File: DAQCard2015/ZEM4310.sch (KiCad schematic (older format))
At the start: 2 parts, among them P1 QTH-090-01-F-D-A, P2 QTH-090-01-F-D-A

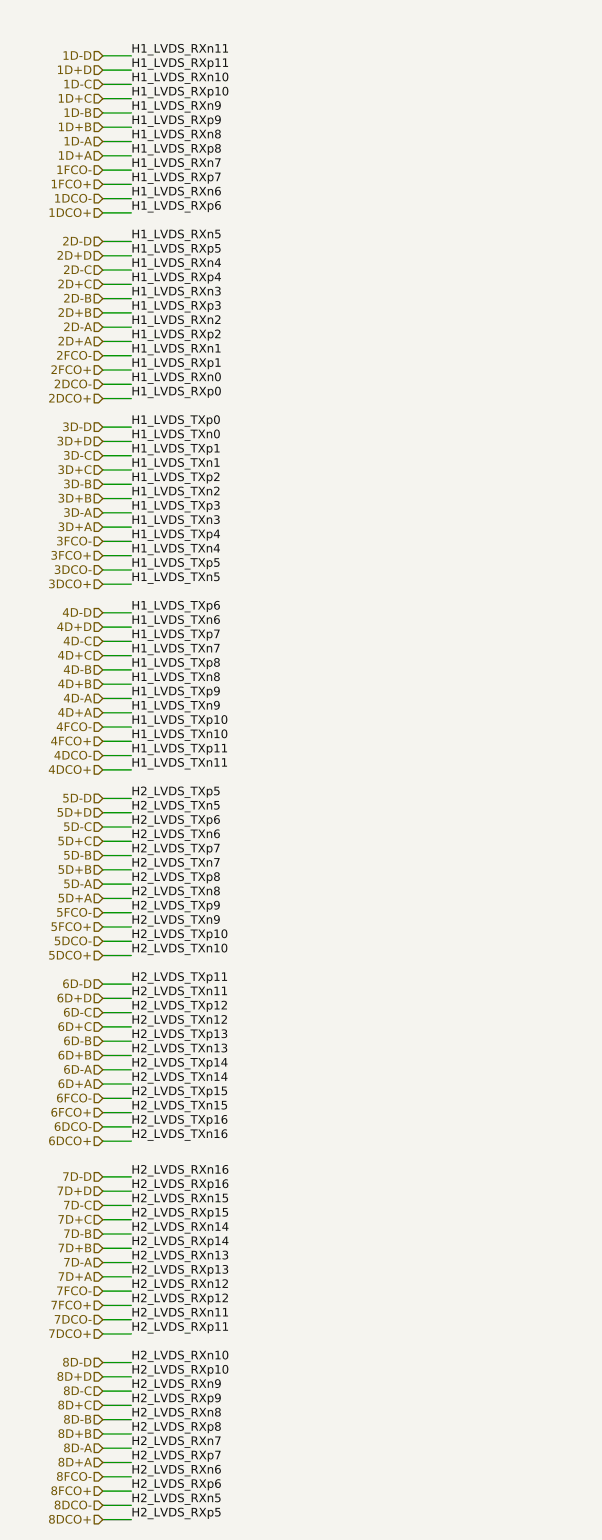
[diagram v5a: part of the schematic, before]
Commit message: Updates to DAQ Board focusing on the power system and flood fills for it
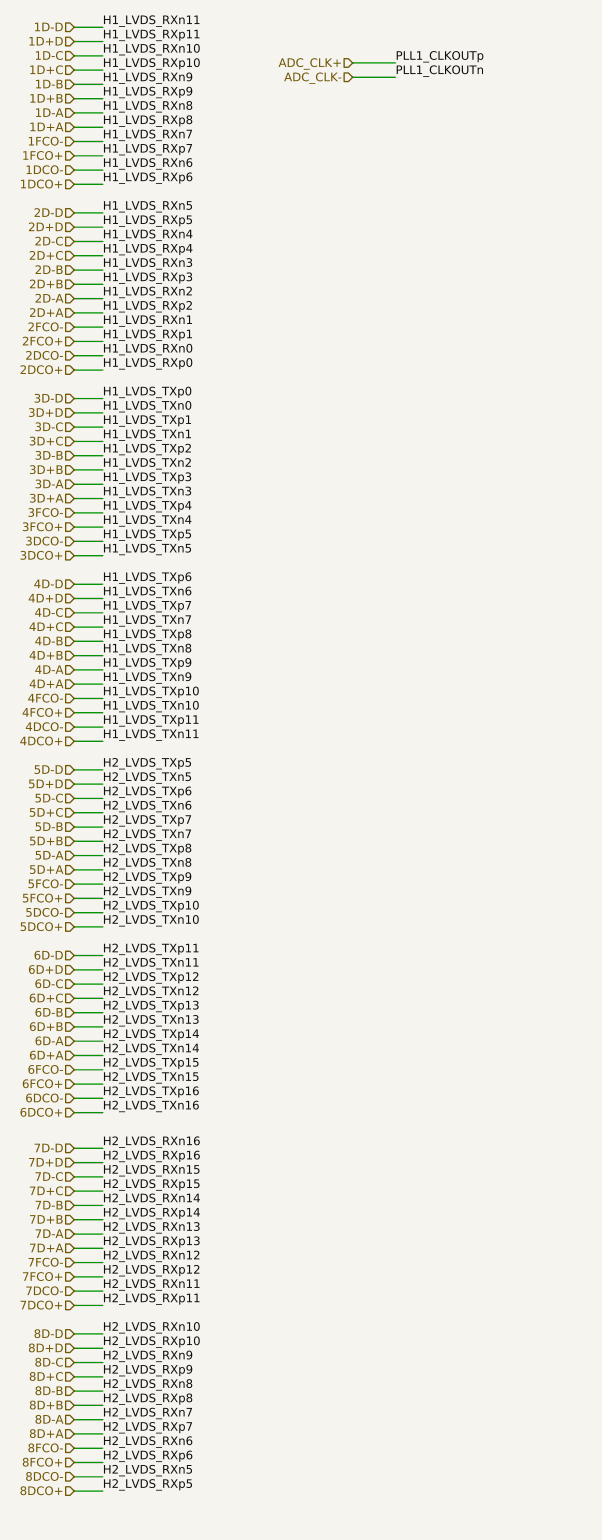
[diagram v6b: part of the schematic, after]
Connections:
- net PLL1_CLKOUTn renamed ADC_CLK-
- net PLL1_CLKOUTp renamed ADC_CLK+

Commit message: Updates to DAQ board focusing on Support electronics
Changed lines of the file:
@@
 $Descr A3 16535 11693
 encoding utf-8
-Sheet 11 13
+Sheet 2 13
 Title ""
 Date ""
@@
 Text GLabel 9400 4750 0    40   Input ~ 0
 3V3dig
-Text HLabel 3050 1000 0    60   Input ~ 0
-ADC_CLK+
-Text HLabel 3050 1100 0    60   Input ~ 0
-ADC_CLK-
 Wire Wire Line
 	3050 1000 3350 1000
@@
 Text Label 3350 1100 0    60   ~ 0
 PLL1_CLKOUTn
+Text GLabel 3050 1000 0    40   Input ~ 0
+ADC_CLK+
+Text GLabel 3050 1100 0    40   Input ~ 0
+ADC_CLK-
 $EndSCHEMATC

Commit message: Adds APC128 connections and voltage supplies
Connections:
- net H1_LVDS_RXn13 renamed RPHI2
- net RPHI2: no longer P1.148
- net H1_LVDS_RXn14 renamed RBO_B4
- net H1_LVDS_RXn15 renamed RBO_B2
- net H1_LVDS_RXn16 renamed RBO_A3
- net H1_LVDS_RXp12 renamed SCL
- net H1_LVDS_RXp13 renamed RPHI1
- net H1_LVDS_RXp14 renamed RBO_A4
- net H1_LVDS_RXp15 renamed RBO_B3
- net H1_LVDS_RXp16 renamed RBO_A2
- net H1_LVDS_TXn12 renamed Reset
- net H1_LVDS_TXn13 renamed SPHI2
- net H1_LVDS_TXn14 renamed SBI
- net H1_LVDS_TXn15 renamed CAL
- net H1_LVDS_TXn16 renamed RBO_B1
- net H1_LVDS_TXp12 renamed IS1
- net H1_LVDS_TXp13 renamed LE
- net H1_LVDS_TXp14 renamed SPHI1
- net H1_LVDS_TXp15 renamed SEB
- net H1_LVDS_TXp16 renamed RBO_A1
- net H2_LVDS_TXn0 renamed CS
- net H2_LVDS_TXn1 renamed SR
- net H2_LVDS_TXp0 renamed RBI
- net H2_LVDS_TXp1 renamed R12
- net H2_LVDS_TXp2 renamed IS2
- new net SDA: P1.148
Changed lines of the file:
@@
 H1_LVDS_RXn11
 Text Label 7400 8950 0    60   ~ 0
-H1_LVDS_RXn13
+H1_LVDS_RXn12
 Text Label 7400 9250 0    60   ~ 0
 H1_LVDS_RXn13
@@
 Text GLabel 3050 1100 0    40   Input ~ 0
 ADC_CLK-
+Text GLabel 3450 8550 0    40   Input ~ 0
+RBI
+Text GLabel 3450 8650 0    40   Input ~ 0
+CS
+Text GLabel 3450 8750 0    40   Input ~ 0
+R12
+Text GLabel 3450 8850 0    40   Input ~ 0
+SR
+Text GLabel 3450 8950 0    40   Input ~ 0
+IS2
+Text GLabel 3450 9050 0    40   Input ~ 0
+IS1
+Text GLabel 3450 9150 0    40   Input ~ 0
+Reset
+Text GLabel 3450 9250 0    40   Input ~ 0
+LE
+Text GLabel 3450 9350 0    40   Input ~ 0
+SPHI2
+Text GLabel 3450 9450 0    40   Input ~ 0
+SPHI1
+Text GLabel 3450 9550 0    40   Input ~ 0
+SBI
+Text GLabel 3450 9650 0    40   Input ~ 0
+SEB
+Text GLabel 3450 9750 0    40   Input ~ 0
+CAL
+Text GLabel 3450 9950 0    40   Input ~ 0
+RBO_B1
+Text GLabel 3450 9850 0    40   Input ~ 0
+RBO_A1
+Text GLabel 3450 10050 0    40   Input ~ 0
+RBO_A3
+Text GLabel 3450 10150 0    40   Input ~ 0
+RBO_A2
+Text GLabel 3450 10250 0    40   Input ~ 0
+RBO_B2
+Text GLabel 3450 10350 0    40   Input ~ 0
+RBO_B3
+Text GLabel 3450 10450 0    40   Input ~ 0
+RBO_B4
+Text GLabel 3450 10550 0    40   Input ~ 0
+RBO_A4
+Text GLabel 3450 10650 0    40   Input ~ 0
+RPHI2
+Text GLabel 3450 10750 0    40   Input ~ 0
+RPHI1
+Text GLabel 3450 10850 0    40   Input ~ 0
+SDA
+Text GLabel 3450 10950 0    40   Input ~ 0
+SCL
+Wire Wire Line
+	3450 10950 3700 10950
+Wire Wire Line
+	3450 10850 3700 10850
+Wire Wire Line
+	3450 10750 3700 10750
+Wire Wire Line
+	3450 10650 3700 10650
+Wire Wire Line
+	3450 10550 3700 10550
+Wire Wire Line
+	3450 10450 3700 10450
+Wire Wire Line
+	3450 10350 3700 10350
+Wire Wire Line
+	3450 10250 3700 10250
+Wire Wire Line
+	3450 10150 3700 10150
+Wire Wire Line
+	3450 10050 3700 10050
+Wire Wire Line
+	3450 9950 3700 9950
+Wire Wire Line
+	3450 9850 3700 9850
+Wire Wire Line
+	3450 9750 3700 9750
+Wire Wire Line
+	3450 9650 3700 9650
+Wire Wire Line
+	3450 9550 3700 9550
+Wire Wire Line
+	3450 9450 3700 9450
+Wire Wire Line
+	3450 9350 3700 9350
+Wire Wire Line
+	3450 9250 3700 9250
+Wire Wire Line
+	3450 9150 3700 9150
+Wire Wire Line
+	3450 9050 3700 9050
+Wire Wire Line
+	3450 8950 3700 8950
+Wire Wire Line
+	3450 8850 3700 8850
+Wire Wire Line
+	3450 8750 3700 8750
+Wire Wire Line
+	3450 8650 3700 8650
+Wire Wire Line
+	3450 8550 3700 8550
+Text Label 3700 10950 0    60   ~ 0
+H1_LVDS_RXp12
+Text Label 3700 10850 0    60   ~ 0
+H1_LVDS_RXn12
+Text Label 3700 10750 0    60   ~ 0
+H1_LVDS_RXp13
+Text Label 3700 10650 0    60   ~ 0
+H1_LVDS_RXn13
+Text Label 3700 10550 0    60   ~ 0
+H1_LVDS_RXp14
+Text Label 3700 10450 0    60   ~ 0
+H1_LVDS_RXn14
+Text Label 3700 10350 0    60   ~ 0
+H1_LVDS_RXp15
+Text Label 3700 10250 0    60   ~ 0
+H1_LVDS_RXn15
+Text Label 3700 10150 0    60   ~ 0
+H1_LVDS_RXp16
+Text Label 3700 10050 0    60   ~ 0
+H1_LVDS_RXn16
+Text Label 3700 9050 0    60   ~ 0
+H1_LVDS_TXp12
+Text Label 3700 9150 0    60   ~ 0
+H1_LVDS_TXn12
+Text Label 3700 9250 0    60   ~ 0
+H1_LVDS_TXp13
+Text Label 3700 9350 0    60   ~ 0
+H1_LVDS_TXn13
+Text Label 3700 9450 0    60   ~ 0
+H1_LVDS_TXp14
+Text Label 3700 9550 0    60   ~ 0
+H1_LVDS_TXn14
+Text Label 3700 9650 0    60   ~ 0
+H1_LVDS_TXp15
+Text Label 3700 9750 0    60   ~ 0
+H1_LVDS_TXn15
+Text Label 3700 9850 0    60   ~ 0
+H1_LVDS_TXp16
+Text Label 3700 9950 0    60   ~ 0
+H1_LVDS_TXn16
+Text Label 3700 8550 0    60   ~ 0
+H2_LVDS_TXp0
+Text Label 3700 8650 0    60   ~ 0
+H2_LVDS_TXn0
+Text Label 3700 8750 0    60   ~ 0
+H2_LVDS_TXp1
+Text Label 3700 8850 0    60   ~ 0
+H2_LVDS_TXn1
+Text Label 3700 8950 0    60   ~ 0
+H2_LVDS_TXp2
 $EndSCHEMATC
